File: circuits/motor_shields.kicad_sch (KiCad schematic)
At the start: 24 parts, among them IC1 BTN70301EPAXUMA1, IC2 BTN70301EPAXUMA1, IC3 BTN70301EPAXUMA1, IC4 BTN70301EPAXUMA1, J4 Conn_01x02_Pin, U2 74HC244

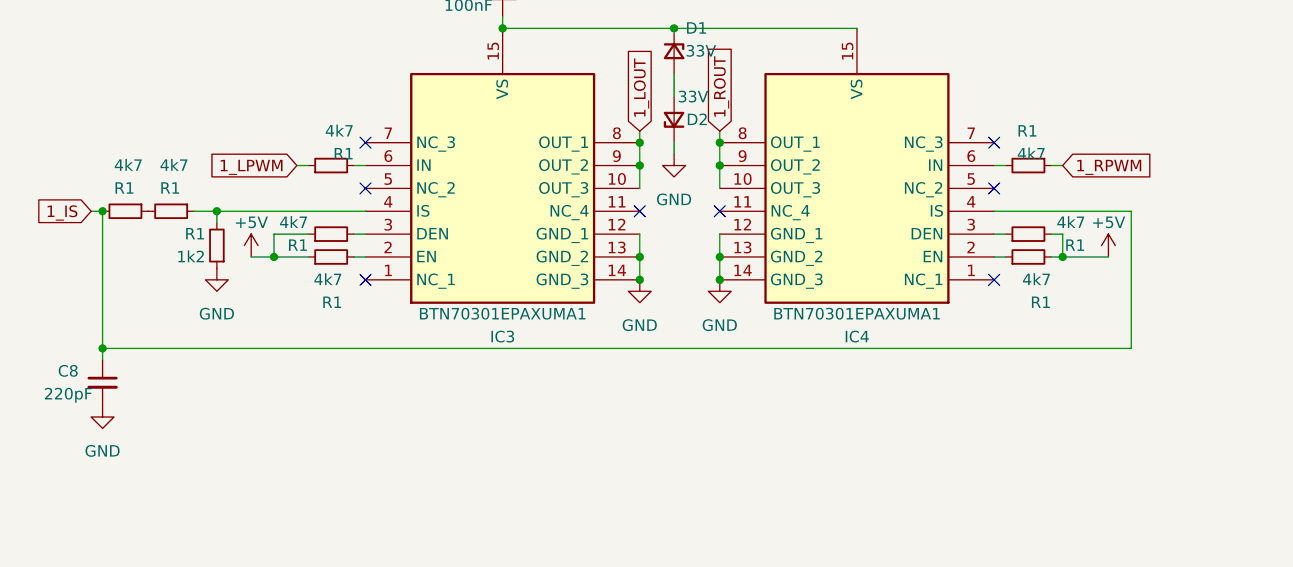
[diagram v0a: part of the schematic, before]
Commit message: updated shield schematic
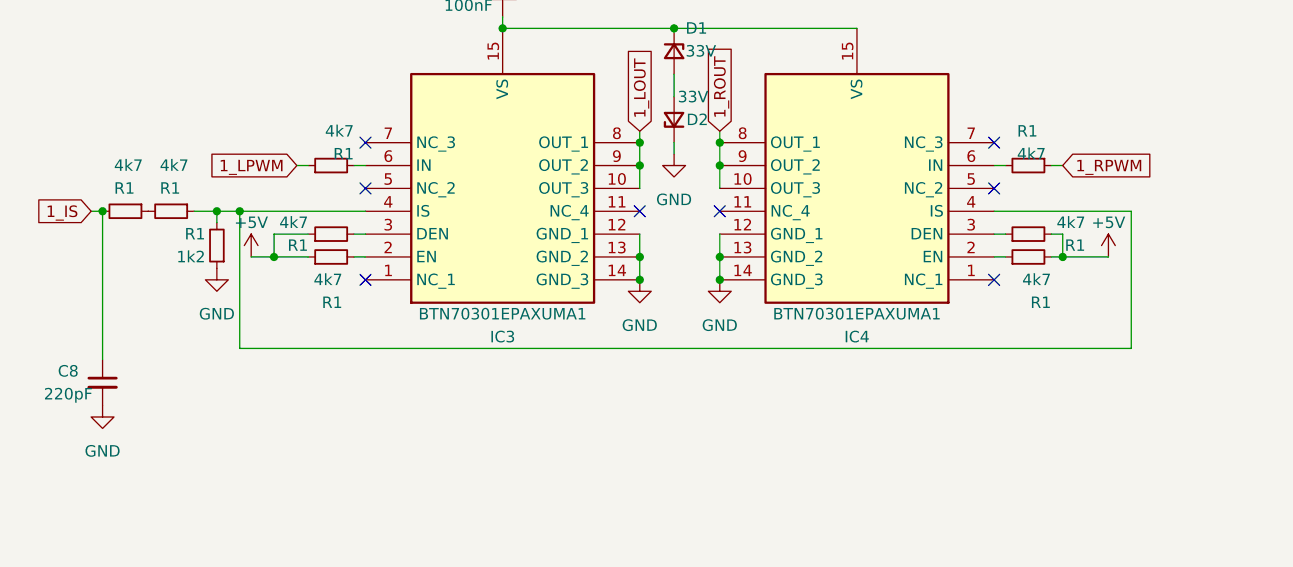
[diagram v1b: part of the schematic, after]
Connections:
- net 1_IS: no longer IC4.4 (IS)
- net at IC3.4 (IS), R1.1, R1.2: now also IC4.4 (IS)
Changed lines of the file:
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@@
   (junction (at 100.33 57.15) (diameter 0) (color 0 0 0 0)
   )
+  (junction (at 46.99 49.53) (diameter 0) (color 0 0 0 0)
+  )
   (junction (at 167.64 123.19) (diameter 0) (color 0 0 0 0)
   )
@@
   )
   (junction (at 167.64 125.73) (diameter 0) (color 0 0 0 0)
-  )
-  (junction (at 31.75 64.77) (diameter 0) (color 0 0 0 0)
   )
   (junction (at 243.84 118.11) (diameter 0) (color 0 0 0 0)
@@
   (no_connect (at 204.47 110.49))
   (no_connect (at 130.81 57.15))
-  (wire (pts (xy 31.75 64.77) (xy 31.75 49.53))
+  (wire (pts (xy 31.75 49.53) (xy 31.75 66.04))
     (stroke (width 0) (type default))
   )
@@
     (stroke (width 0) (type default))
   )
+  (wire (pts (xy 46.99 64.77) (xy 46.99 49.53))
+    (stroke (width 0) (type default))
+  )
   (wire (pts (xy 173.99 97.79) (xy 175.26 97.79))
     (stroke (width 0) (type default))
@@
     (stroke (width 0) (type default))
   )
-  (wire (pts (xy 60.96 49.53) (xy 44.45 49.53))
+  (wire (pts (xy 60.96 49.53) (xy 46.99 49.53))
     (stroke (width 0) (type default))
   )
@@
     (stroke (width 0) (type default))
   )
-  (wire (pts (xy 146.05 64.77) (xy 31.75 64.77))
-    (stroke (width 0) (type default))
-  )
   (wire (pts (xy 91.44 54.61) (xy 91.44 57.15))
     (stroke (width 0) (type default))
@@
     (stroke (width 0) (type default))
   )
+  (wire (pts (xy 146.05 64.77) (xy 46.99 64.77))
+    (stroke (width 0) (type default))
+  )
   (wire (pts (xy 149.86 107.95) (xy 167.64 107.95))
     (stroke (width 0) (type default))
@@
     (stroke (width 0) (type default))
   )
-  (wire (pts (xy 31.75 64.77) (xy 31.75 66.04))
-    (stroke (width 0) (type default))
-  )
   (wire (pts (xy 30.48 49.53) (xy 31.75 49.53))
     (stroke (width 0) (type default))
@@
     (stroke (width 0) (type default))
   )
+  (wire (pts (xy 46.99 49.53) (xy 44.45 49.53))
+    (stroke (width 0) (type default))
+  )

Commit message: controller pcb rev 1
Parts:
- removed C7: 1u, symbol Device:C_Small
- removed D1, D2: 33V, symbol Device:D_Zener_Small
- removed IC1: BTN70301EPAXUMA1, SOP65P600X115-15N, symbol SamacSys_Parts:BTN70301EPAXUMA1
- removed J4: Conn_01x02_Pin, symbol Connector:Conn_01x02_Pin
- removed R1 (x4): 1k, symbol Device:R_Small
- removed U2: 74HC244, symbol 74xx:74HC244
- added C10, C13, C14: 100nF, Capacitor_SMD:C_0603_1608Metric_Pad1.08x0.95mm_HandSolder, symbol Device:C_Small
- added C11, C12, C8: 220pF, Capacitor_SMD:C_0402_1005Metric_Pad0.74x0.62mm_HandSolder, symbol Device:C_Small
- added IC4, IC5, IC6, IC7, IC8: BTN70301EPAXUMA1, rbc Custom Library:Infineon_PG-TSDSO-14-22_custom, symbol SamacSys_Parts:BTN70301EPAXUMA1
- added J4, J5, J7, J8: Conn_01x06_Pin, Connector_Molex:Molex_Micro-Fit_3.0_43045-0612_2x03_P3.00mm_Vertical, symbol Connector:Conn_01x06_Pin
- added J6, J9: Conn_01x02_Pin, TerminalBlock_Phoenix:TerminalBlock_Phoenix_MKDS-3-2-5.08_1x02_P5.08mm_Horizontal, symbol Connector:Conn_01x02_Pin
- added R? (x24): 4k7, Resistor_SMD:R_1206_3216Metric_Pad1.30x1.75mm_HandSolder, symbol Device:R_Small
- added R? (x3): 1k2, Resistor_SMD:R_1206_3216Metric_Pad1.30x1.75mm_HandSolder, symbol Device:R_Small
- C7: renamed from C8; footprint (none) -> Capacitor_SMD:C_0402_1005Metric_Pad0.74x0.62mm_HandSolder
- C9: footprint (none) -> Capacitor_SMD:C_0603_1608Metric_Pad1.08x0.95mm_HandSolder
- IC1: renamed from IC3; footprint SOP65P600X115-15N -> rbc Custom Library:Infineon_PG-TSDSO-14-22_custom
- IC2: footprint SOP65P600X115-15N -> rbc Custom Library:Infineon_PG-TSDSO-14-22_custom
- IC3: renamed from IC4; footprint SOP65P600X115-15N -> rbc Custom Library:Infineon_PG-TSDSO-14-22_custom
- R? (x9): renamed from R1; footprint (none) -> Resistor_SMD:R_1206_3216Metric_Pad1.30x1.75mm_HandSolder
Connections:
- net +12V: now also IC1.15 (VS), IC2.15 (VS), IC3.15 (VS), C10.2, IC4.15 (VS), J6.1 (Pin_1)
- net +5V: now also J4.2 (Pin_2), J5.2 (Pin_2), J7.2 (Pin_2), J8.2 (Pin_2), R?.1, R?.1, R?.1, R?.1, R?.1, R?.1, R?.2, R?.2, R?.2, R?.2, R?.2, R?.2; no longer IC2.3 (DEN)
- net 1_LOUT: now also J4.4 (Pin_4)
- net 1_ROUT: now also J4.6 (Pin_6)
- net GND: now also C9.2, C10.1, C11.2, C12.2, C13.1, C14.1, C8.2, IC4.12 (GND_1), IC4.13 (GND_2), IC4.14 (GND_3), IC5.12 (GND_1), IC5.13 (GND_2), IC5.14 (GND_3), IC6.12 (GND_1), IC6.13 (GND_2), IC6.14 (GND_3), IC7.12 (GND_1), IC7.13 (GND_2), IC7.14 (GND_3), IC8.12 (GND_1), IC8.13 (GND_2), IC8.14 (GND_3), J4.5 (Pin_5), J5.5 (Pin_5), J6.2 (Pin_2), J7.5 (Pin_5), J8.5 (Pin_5), J9.2 (Pin_2), R?.1, R?.1, R?.1
- net at IC2.2 (EN): now also R?.2
- net at IC2.6 (IN): now also R?.2
- net 2_LOUT: now reaches IC2.10 (OUT_3), IC2.8 (OUT_1), IC2.9 (OUT_2)
- net 2_LOUT: now also J5.4 (Pin_4)
- net at IC2.4 (IS): now also IC4.4 (IS), R?.1, R?.2
- new net: R?.1, R?.2 (x3)
- new net: IC5.6 (IN), R?.2
- new net: IC8.2 (EN), R?.1
- new net: IC5.4 (IS), IC7.4 (IS), R?.1, R?.2
- new net: IC5.3 (DEN), R?.2
- new net: IC7.6 (IN), R?.2
- new net: IC6.4 (IS), IC8.4 (IS), R?.1, R?.2
- new net: IC4.6 (IN), R?.2
- new net: IC7.2 (EN), R?.1
- new net: IC7.3 (DEN), R?.1
- new net: IC8.6 (IN), R?.2
- new net: IC8.3 (DEN), R?.1
- new net: IC6.2 (EN), R?.2
- new net: IC6.3 (DEN), R?.2
- new net: IC6.6 (IN), R?.2
- new net: IC2.3 (DEN), R?.2
- new net: IC5.2 (EN), R?.2
- new net: IC4.2 (EN), R?.1
- new net: IC4.3 (DEN), R?.1
- new net +12P: C13.2, C14.2, IC5.15 (VS), IC6.15 (VS), IC7.15 (VS), IC8.15 (VS), J9.1 (Pin_1)
- new net 1_HALL_A: J4.1 (Pin_1)
- new net 1_HALL_B: J4.3 (Pin_3)
- new net 2_HALL_A: J5.1 (Pin_1)
- new net 2_HALL_B: J5.3 (Pin_3)
- new net 2_IS: C8.1, R?.2
- new net 2_LPWM: R?.1
- new net 2_ROUT: IC4.10 (OUT_3), IC4.8 (OUT_1), IC4.9 (OUT_2), J5.6 (Pin_6)
- new net 2_RPWM: R?.1
- new net 3_HALL_A: J8.1 (Pin_1)
- new net 3_HALL_B: J8.3 (Pin_3)
- new net 3_IS: C12.1, R?.2
- new net 3_LOUT: IC6.10 (OUT_3), IC6.8 (OUT_1), IC6.9 (OUT_2), J8.4 (Pin_4)
- new net 3_LPWM: R?.1
- new net 3_ROUT: IC8.10 (OUT_3), IC8.8 (OUT_1), IC8.9 (OUT_2), J8.6 (Pin_6)
- new net 3_RPWM: R?.1
- new net 4_HALL_A: J7.1 (Pin_1)
- new net 4_HALL_B: J7.3 (Pin_3)
- new net 4_IS: C11.1, R?.2
- new net 4_LOUT: IC5.10 (OUT_3), IC5.8 (OUT_1), IC5.9 (OUT_2), J7.4 (Pin_4)
- new net 4_LPWM: R?.1
- new net 4_ROUT: IC7.10 (OUT_3), IC7.8 (OUT_1), IC7.9 (OUT_2), J7.6 (Pin_6)
- new net 4_RPWM: R?.1
- no-connect marks 16 -> 32
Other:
- note added: "Motor 1"
- note added: "Motor 2"
- note added: "Motor 3"
- note added: "Motor 4"
- moved on the sheet: C7, C9, IC1, IC3, R?

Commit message: PCB Rev2.0 publish
It's here
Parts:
- removed C11: 220pF, Capacitor_SMD:C_0402_1005Metric_Pad0.74x0.62mm_HandSolder, symbol Device:C_Small
- removed C13: 100nF, Capacitor_SMD:C_0603_1608Metric_Pad1.08x0.95mm_HandSolder, symbol Device:C_Small
- removed IC5, IC7: BTN70301EPAXUMA1, rbc Custom Library:Infineon_PG-TSDSO-14-22_custom, symbol SamacSys_Parts:BTN70301EPAXUMA1
- removed J6, J9: Conn_01x02_Pin, TerminalBlock_Phoenix:TerminalBlock_Phoenix_MKDS-3-2-5.08_1x02_P5.08mm_Horizontal, symbol Connector:Conn_01x02_Pin
- removed J7: Conn_01x06_Pin, Connector_Molex:Molex_Micro-Fit_3.0_43045-0612_2x03_P3.00mm_Vertical, symbol Connector:Conn_01x06_Pin
- removed R? (x8): 4k7, Resistor_SMD:R_1206_3216Metric_Pad1.30x1.75mm_HandSolder, symbol Device:R_Small
- removed R?: 1k2, Resistor_SMD:R_1206_3216Metric_Pad1.30x1.75mm_HandSolder, symbol Device:R_Small
- C28: renamed from C7; value 220pF -> 220nF; footprint Capacitor_SMD:C_0402_1005Metric_Pad0.74x0.62mm_HandSolder -> Capacitor_SMD:C_0805_2012Metric
- C29: renamed from C8; value 220pF -> 220nF; footprint Capacitor_SMD:C_0402_1005Metric_Pad0.74x0.62mm_HandSolder -> Capacitor_SMD:C_0805_2012Metric
- C30: renamed from C9; footprint Capacitor_SMD:C_0603_1608Metric_Pad1.08x0.95mm_HandSolder -> Capacitor_SMD:C_0402_1005Metric
- C31: renamed from C10; footprint Capacitor_SMD:C_0603_1608Metric_Pad1.08x0.95mm_HandSolder -> Capacitor_SMD:C_0402_1005Metric
- C32: renamed from C12; value 220pF -> 220nF; footprint Capacitor_SMD:C_0402_1005Metric_Pad0.74x0.62mm_HandSolder -> Capacitor_SMD:C_0805_2012Metric
- C33: renamed from C14; footprint Capacitor_SMD:C_0603_1608Metric_Pad1.08x0.95mm_HandSolder -> Capacitor_SMD:C_0402_1005Metric
- R? (x27): footprint Resistor_SMD:R_1206_3216Metric_Pad1.30x1.75mm_HandSolder -> Resistor_SMD:R_1206_3216Metric
- renumbered IC6 to IC10, IC8 to IC11, IC1 to IC6, IC2 to IC7, IC3 to IC8, IC4 to IC9, J5 to J10, J8 to J11, J4 to J9
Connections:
- net +12V: no longer C31.2, IC7.15 (VS), IC9.15 (VS)
- net +5V: no longer R?.1, R?.1, R?.1, R?.1, R?.1, R?.1, R?.2, R?.2, R?.2, R?.2, R?.2, R?.2
- new net +12C: C31.2, IC7.15 (VS), IC9.15 (VS)
- new net M_EN_DEN: R?.1, R?.1, R?.1, R?.1, R?.1, R?.1, R?.2, R?.2, R?.2, R?.2, R?.2, R?.2
- no-connect marks 32 -> 24
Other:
- note removed: "Motor 4"
- title: (none) -> RBC by UGS
- moved on the sheet: C28, C29, C30, C31, C32, C33, IC10, IC11, IC6, IC7, IC8, IC9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
